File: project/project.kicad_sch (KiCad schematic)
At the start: 11 parts, among them J101 BUS, J102 BUS, J103 Back, U101 GX101

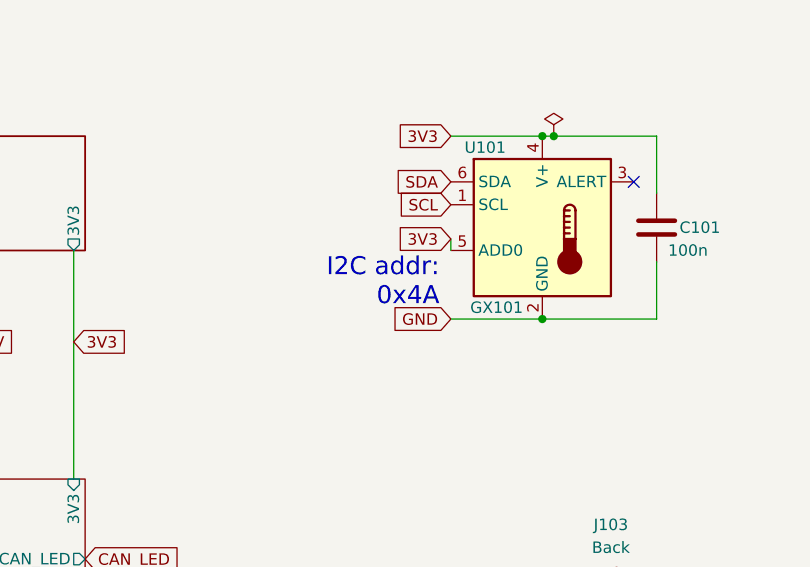
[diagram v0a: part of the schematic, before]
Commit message: fixes after preliminary testing
* Switching to TMP102 as TMP101 is no longer available
* Removing 5V LDO with OVP as it caused more problems
* bumping up version
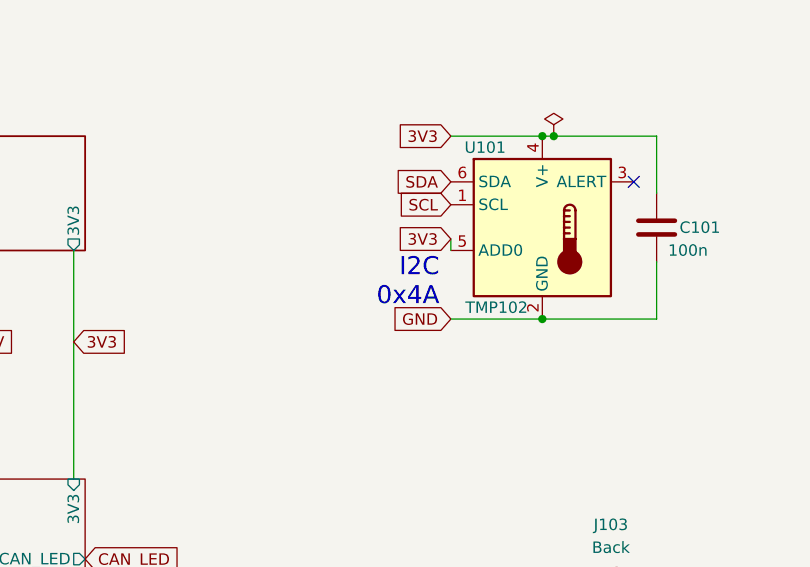
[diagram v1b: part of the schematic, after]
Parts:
- U101: value GX101 -> TMP102; footprint Package_TO_SOT_SMD:SOT-23-6 -> -local:SOT-563; lcsc# C5441728 -> C99269
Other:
- note added: "I2C 0x4A"
- note removed: "I2C addr: 0x4A"

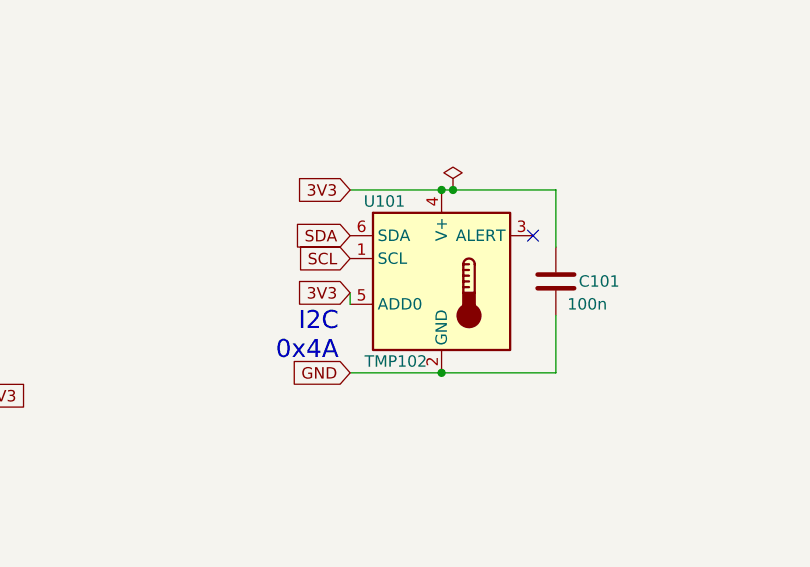
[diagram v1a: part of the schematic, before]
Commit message: fixing tmp102 pinout
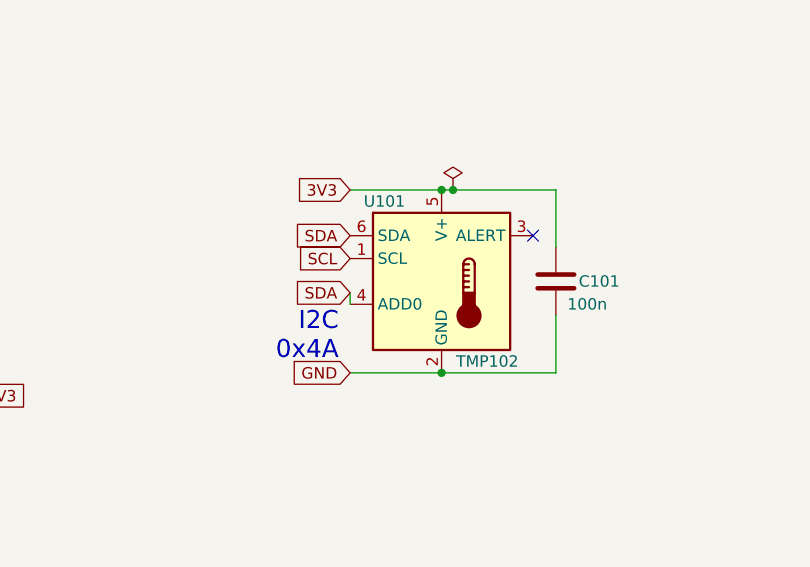
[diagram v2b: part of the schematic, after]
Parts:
- U101: symbol Sensor_Temperature:TMP101 -> Sensor_Temperature:TMP102xxDRL
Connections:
- net 3V3: no longer U101.4 (V+)
- net SDA: now also U101.4 (ADD0)
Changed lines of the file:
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@@
     )
   )
-  (global_label "3V3" (shape input) (at 167.64 62.23 180) (fields_autoplaced)
+  (global_label "SDA" (shape input) (at 167.64 62.23 180) (fields_autoplaced)
     (effects (font (size 1.27 1.27)) (justify right))
-    (property "Intersheet References" "${INTERSHEET_REFS}" (id 0) (at 161.7193 62.1506 0)
+    (property "Intersheet References" "${INTERSHEET_REFS}" (id 0) (at 161.6588 62.1506 0)
       (effects (font (size 1.27 1.27)) (justify right) hide)
     )
@@
     )
   )
-  (symbol (lib_id "Sensor_Temperature:TMP101") (at 177.8 60.96 0) (unit 1)
+  (symbol (lib_id "Sensor_Temperature:TMP102xxDRL") (at 177.8 60.96 0) (unit 1)
     (in_bom yes) (on_board yes)
     (property "Reference" "U101" (id 0) (at 171.45 52.07 0))
-    (property "Value" "TMP102" (id 1) (at 172.72 69.85 0))
+    (property "Value" "TMP102" (id 1) (at 182.88 69.85 0))
     (property "Footprint" "-local:SOT-563" (id 2) (at 179.07 69.85 0)
       (effects (font (size 1.27 1.27)) (justify left) hide)
     )
-    (property "Datasheet" "https://www.lcsc.com/datasheet/C99269.pdf" (id 3) (at 179.07 72.39 0)
+    (property "Datasheet" "https://www.ti.com/lit/ds/symlink/tmp102.pdf" (id 3) (at 179.07 72.39 0)
       (effects (font (size 1.27 1.27)) (justify left) hide)
     )
